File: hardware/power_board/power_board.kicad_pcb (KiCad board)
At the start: 2 copper layers, 104.1 x 77.9 mm, 35 parts, among them J1 MCU, J2 MAINS_IN, J6 HEATER-E, J7 HEATER-N, J8 HEATER-L, K3 HEATER-BOTTOM, K4 HEATER-TOP, Q4 MMBT3904, Q5 MMBT3904, U10 PC817, U6 AMS1117-3.3, U9 PC817

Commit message: v2 Power/Relay PCB
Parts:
- removed D6, D7: LED, LED_THT:LED_D5.0mm_Clear
- removed J6: HEATER-E, TerminalBlock_Dinkle:TerminalBlock_Dinkle_DT-55-B01X-02_P10.00mm
- removed J7: HEATER-N, TerminalBlock_Dinkle:TerminalBlock_Dinkle_DT-55-B01X-02_P10.00mm
- removed R12, R13: 330, Resistor_SMD:R_0805_2012Metric
- added C2: 470uF, Capacitor_THT:CP_Radial_D8.0mm_P3.50mm, F.Cu at (157.1, 92.3)
- added C3: 1uF, Capacitor_THT:CP_Radial_D8.0mm_P3.50mm, F.Cu at (166.4, 92.2)
- added Q1: MMBT3904, Package_TO_SOT_SMD:SOT-23, B.Cu at (126.0, 72.5)
- added R2: 1k, Resistor_SMD:R_0805_2012Metric, B.Cu at (130.1, 71.9)
- D3: renamed from D1; footprint LED_THT:LED_D5.0mm_Clear -> LED_SMD:LED_0805_2012Metric_Pad1.15x1.40mm_HandSolder; moved to B.Cu
- F1: renamed from F3; footprint TE5:FUSE_BK_PCE-5-R -> Fuse:Fuse_Littelfuse_395Series
- J1: footprint Connector_PinHeader_2.54mm:PinHeader_1x04_P2.54mm_Vertical -> Connector_PinHeader_2.54mm:PinHeader_1x06_P2.54mm_Vertical
- J2: footprint TerminalBlock_Dinkle:TerminalBlock_Dinkle_DT-55-B01X-03_P10.00mm -> TerminalBlock_Dinkle:TerminalBlock_Dinkle_DT-55-B01X-02_P10.00mm
- J8: value HEATER-L -> HEATER; footprint TerminalBlock_Dinkle:TerminalBlock_Dinkle_DT-55-B01X-02_P10.00mm -> TerminalBlock_Dinkle:TerminalBlock_Dinkle_DT-55-B01X-03_P10.00mm
- K1: renamed from K4; footprint Relay_THT:Relay_SPDT_RAYEX-L90 -> Relay_THT:Relay_SPST_RAYEX-L90A
- K2: renamed from K3; footprint Relay_THT:Relay_SPDT_RAYEX-L90 -> Relay_THT:Relay_SPST_RAYEX-L90A
- U1: renamed from U9; footprint Package_DIP:DIP-4_W7.62mm -> Package_DIP:DIP-4_W7.62mm_SMDSocket_SmallPads; moved to B.Cu
- U2: renamed from U10; footprint Package_DIP:DIP-4_W7.62mm -> Package_DIP:DIP-4_W7.62mm_SMDSocket_SmallPads; moved to B.Cu
- moved REF** 253.2 mm to (-125.6, 142.2)
- moved REF** 248.7 mm to (-117.5, 141.6)
- moved REF** 175.8 mm to (-136.8, 142.4)
- moved REF** 164.1 mm to (-131.1, 142.2)
- moved J1 156.6 mm to (176.4, 71.2)
- moved C1 151.4 mm to (181.3, 131.2)
- moved C4 138.5 mm to (161.9, 84.0), turned to 0 degrees
- moved D3 136.1 mm to (173.9, 89.4), turned to 0 degrees
- moved U3 133.9 mm to (161.7, 78.1)
- moved C5 130.3 mm to (167.3, 78.2), turned to -90 degrees
- moved R8 127.7 mm to (173.8, 93.5), turned to 0 degrees
- moved L1 127.6 mm to (172.3, 131.5)
- moved RV1 126.3 mm to (155.8, 125.5), turned to 90 degrees
- moved F1 116.1 mm to (155.7, 131.7), turned to 0 degrees
- moved PS1 115.7 mm to (156.0, 103.5), turned to 0 degrees
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- renumbered C4 to C1, C5 to C4, C6 to C5, D9 to D1, D8 to D2, L2 to L1, PS2 to PS1, Q5 to Q2, Q4 to Q3, R8 to R1, R10 to R3, R9 to R5, R11 to R6, R1 to R8, RV2 to RV1, U6 to U3
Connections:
- D1 pad 1: +3.3V -> +5V
- D1 pad 2: Net-(D9-A) -> LED_TOP
- D2 pad 1: +3.3V -> +5V
- D2 pad 2: Net-(D8-A) -> LED_BOTTOM
- J1 pad 1: RELAY_TOP -> LED_BOTTOM
- J1 pad 3: +3.3V -> LED_TOP
- J1 pad 4: GND -> RELAY_TOP
- J2 pad 1: MAINSIN_N -> MAINSIN_L
- J2 pad 2: MAINSIN_L -> MAINSIN_N
- K1 pad A1: +3.3V -> +5V
- K1 pad A2: Net-(D9-A) -> LED_TOP
- K2 pad A1: +3.3V -> +5V
- K2 pad A2: Net-(D8-A) -> LED_BOTTOM
- Q2 pad 3: Net-(D9-A) -> LED_TOP
- Q3 pad 3: Net-(D8-A) -> LED_BOTTOM
- U1 pad 4: +3.3V -> +5V
- U2 pad 4: +3.3V -> +5V
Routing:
- net +3.3V: track 212.2 -> 24.4 mm, vias 2 -> 0
- net LED_BOTTOM: track 0.00 -> 109.7 mm
- net +5V: track 64.5 -> 162.1 mm
- net LED_TOP: track 0.00 -> 68.7 mm
- net Net-(K3-Pad12): track 56.9 -> 0.00 mm
- net RELAY_TOP: track 97.0 -> 51.8 mm, vias 0 -> 2
- net Net-(J8-Pin_1): track 63.2 -> 20.1 mm
- net MAINSIN_N: track 113.4 -> 80.6 mm
- net MAINSIN_E: track 23.9 -> 0.00 mm
- net Net-(D8-A): track 21.2 -> 0.00 mm
- net Net-(D9-A): track 21.0 -> 0.00 mm
- net Net-(R3-Pad1): track 3.61 -> 21.5 mm
- net Net-(R6-Pad1): track 3.79 -> 18.8 mm
- net MAINSIN_L: track 82.3 -> 68.4 mm
- net Net-(D7-K): track 10.2 -> 0.00 mm
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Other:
- board size 104.1 x 77.9 mm -> 101.3 x 70.6 mm
- board text added: "L-BOTTOM"
- board text added: "L-TOP"
- board text added: "N-HEATERS"

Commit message: Refactored PCBs for v2. See README
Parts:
- removed the REF** at (-117.5, 141.6)
- removed the REF** at (-131.1, 142.2)
- removed the REF** at (-136.8, 142.4)
- removed the REF** at (-125.6, 142.2)
- added REF**: MountingHole_2.2mm_M2_DIN965_Pad, MountingHole:MountingHole_2.2mm_M2_DIN965_Pad, F.Cu at (190.8, 136.3)
- added REF**: MountingHole_2.2mm_M2_DIN965_Pad, MountingHole:MountingHole_2.2mm_M2_DIN965_Pad, F.Cu at (97.2, 136.3)
- added REF**: MountingHole_2.2mm_M2_DIN965_Pad, MountingHole:MountingHole_2.2mm_M2_DIN965_Pad, F.Cu at (97.7, 68.9)
- J2: footprint TerminalBlock_Dinkle:TerminalBlock_Dinkle_DT-55-B01X-02_P10.00mm -> TerminalBlock2:HB9500-9.5-2P
- J8: footprint TerminalBlock_Dinkle:TerminalBlock_Dinkle_DT-55-B01X-03_P10.00mm -> TerminalBlock2:HB9500-9.5-3P
- L1: footprint Inductor_THT:Choke_Schaffner_RN204-04-9.0x14.0mm -> Chokes:CHOKE UU9.8
- U1, U2: footprint Package_DIP:DIP-4_W7.62mm_SMDSocket_SmallPads -> PC817XI:SOIC254P975X460-4N
- moved J2 18.8 mm to (128.2, 117.4), turned to 0 degrees
- moved L1 12.3 mm to (177.8, 120.5), turned to -90 degrees
- moved J8 9.50 mm to (96.4, 117.3)
- moved F1 3.04 mm to (157.6, 134.0)
- moved PS1 3.04 mm to (158.0, 105.8)
- moved RV1 3.04 mm to (157.8, 127.8)
- moved C1 2.35 mm to (183.4, 132.3)
- moved C2 1.80 mm to (158.9, 92.3)
- moved D3 1.80 mm to (175.7, 89.4)
- moved R8 1.80 mm to (175.6, 93.5)
- moved K2 1.80 mm to (110.7, 88.2)
- moved C3 1.80 mm to (168.2, 92.2)
- moved K1 1.80 mm to (140.1, 88.3)
- moved R1 0.91 mm to (147.4, 75.3)
- moved C4 0.91 mm to (161.0, 83.9)
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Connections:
- J2 pad 1: MAINSIN_L -> MAINSIN_N
- J2 pad 2: MAINSIN_N -> MAINSIN_L
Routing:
- net Net-(PS1-AC/N): track 28.6 -> 18.9 mm
- net GND: track 168.5 -> 177.4 mm
- net Net-(PS1-AC/L): track 23.2 -> 30.8 mm
- net MAINSIN_L: track 68.4 -> 74.9 mm
- net Net-(J8-Pin_1): track 20.1 -> 15.5 mm
- net MAINSIN_N: track 80.6 -> 84.5 mm
- net +5V: track 162.1 -> 165.6 mm
- net Net-(J8-Pin_2): track 28.7 -> 31.0 mm
- net Net-(C1-Pad1): track 32.9 -> 31.3 mm
- net LED_TOP: track 68.7 -> 69.4 mm
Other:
- board size 101.3 x 70.6 mm -> 98.8 x 72.8 mm

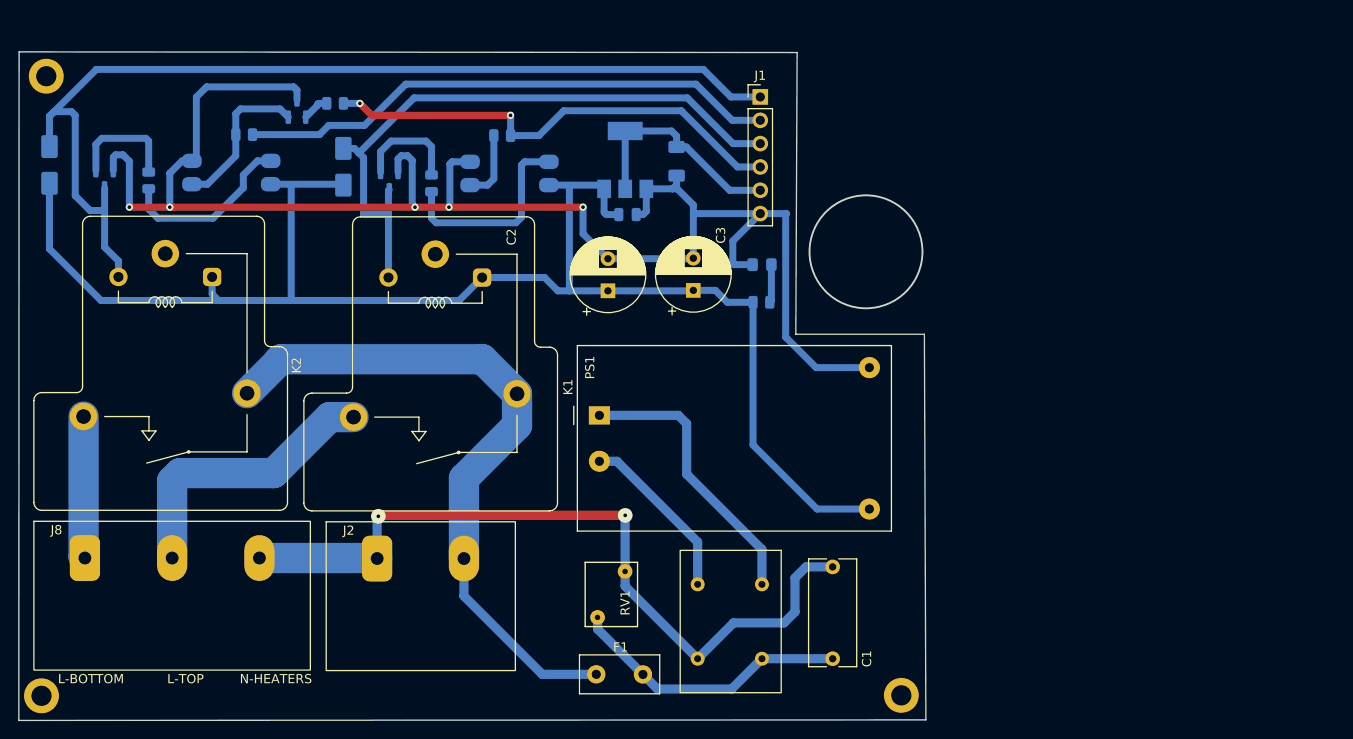
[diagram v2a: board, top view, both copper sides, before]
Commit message: v2 layout changes to fit in bax
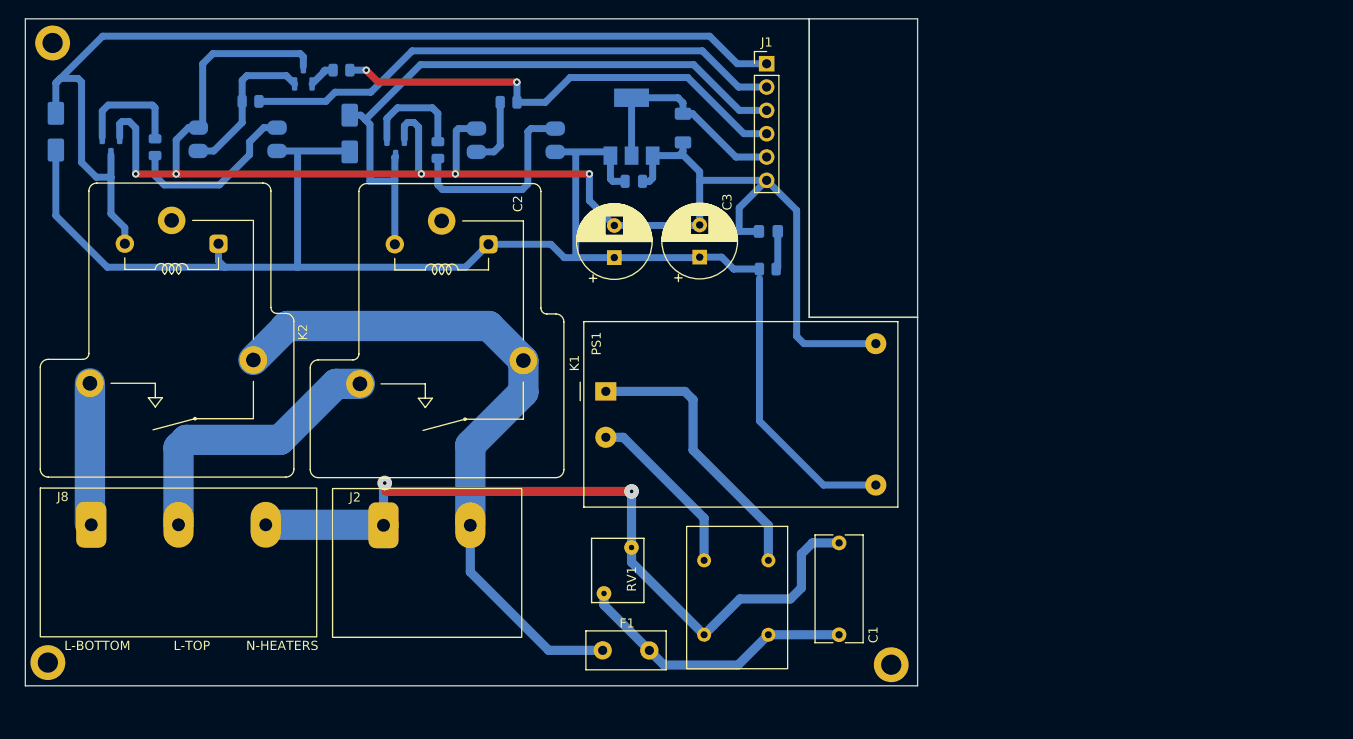
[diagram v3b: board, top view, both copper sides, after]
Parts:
- moved C3 3.69 mm to (168.9, 88.6)
- moved R1 3.69 mm to (148.1, 71.7)
- moved J8 3.69 mm to (97.1, 113.7)
- moved C2 3.69 mm to (159.6, 88.6)
- moved D2 3.69 mm to (98.8, 74.9)
- moved D3 3.69 mm to (176.4, 85.8)
- moved J1 3.69 mm to (176.2, 67.5)
- moved J2 3.69 mm to (128.9, 113.8)
- moved K1 3.69 mm to (140.8, 84.6)
- moved K2 3.69 mm to (111.4, 84.6)
- moved Q1 3.69 mm to (125.7, 68.8)
- moved Q3 3.69 mm to (104.8, 76.5)
- moved R2 3.69 mm to (129.9, 68.2)
- moved R3 3.69 mm to (140.4, 76.9)
- moved R6 3.69 mm to (109.6, 76.6)
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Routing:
- net MAINSIN_L: track 74.9 -> 76.0 mm
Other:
- board size 98.8 x 72.8 mm -> 97.2 x 72.6 mm

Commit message: v2 Boards for fabrication
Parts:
- C1, C2, C3, F1, J1, J2, J8, K1, K2, L1, PS1, REF** (x3), RV1: moved to B.Cu
- C4, C5, D1, D2, D3, Q1, Q2, Q3, R1, R2, R3, R5, R6, R8, U1, U2, U3: moved to F.Cu
- moved J8 93.5 mm to (190.6, 113.7), turned to 180 degrees
- moved REF** 91.8 mm to (97.9, 133.0), turned to 180 degrees
- moved REF** 91.8 mm to (189.7, 132.7), turned to 180 degrees
- moved REF** 90.8 mm to (189.2, 65.3), turned to 180 degrees
- moved D2 90.1 mm to (188.9, 74.9)
- moved C1 80.5 mm to (103.6, 129.7)
- moved Q3 78.1 mm to (182.9, 76.5)
- moved L1 69.3 mm to (109.2, 117.9)
- moved R6 68.5 mm to (178.1, 76.6)
- moved D3 65.1 mm to (111.3, 85.8), turned to 180 degrees
- moved R8 64.9 mm to (111.4, 89.9), turned to 180 degrees
- moved K2 64.9 mm to (176.3, 84.6)
- moved J1 64.7 mm to (111.5, 67.5), turned to 180 degrees
- moved U2 50.5 mm to (169.1, 75.8), turned to 180 degrees
- moved C3 50.1 mm to (118.8, 88.6)
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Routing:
- net MAINSIN_N: track 84.5 -> 83.2 mm
- added copper zone on F.Cu, net (none)
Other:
- outline, holes or cut-outs redrawn

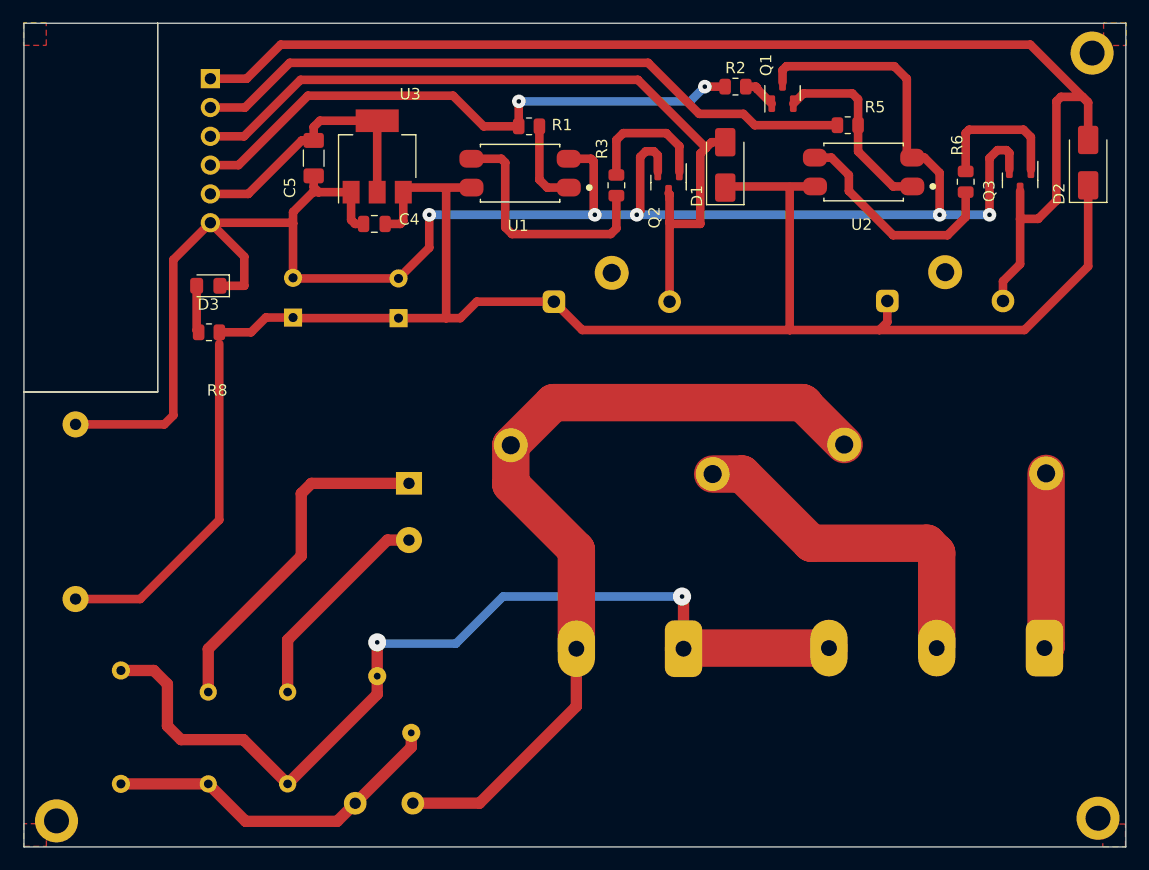
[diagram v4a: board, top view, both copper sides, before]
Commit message: Add missing holes and fabrication marks
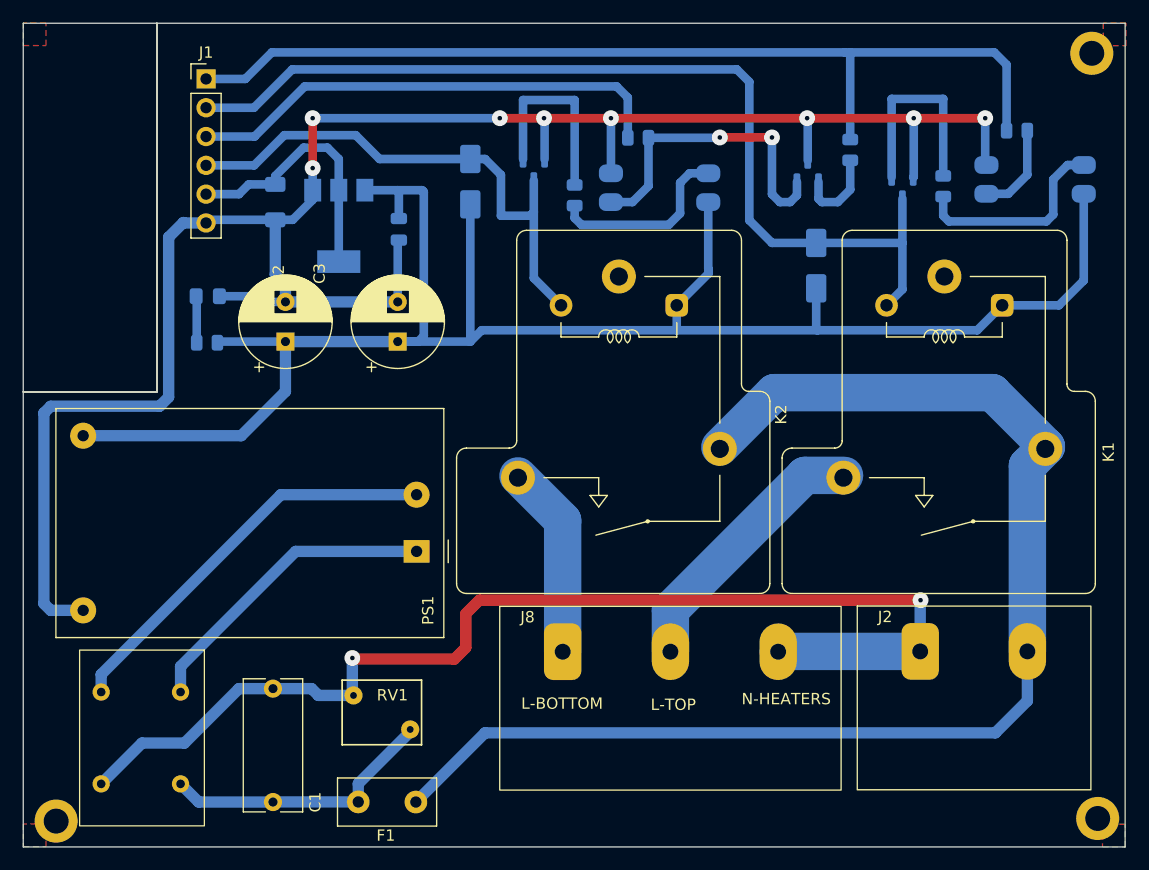
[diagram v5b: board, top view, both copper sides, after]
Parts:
- removed REF** (x3): MountingHole_2.2mm_M2_DIN965_Pad, MountingHole:MountingHole_2.2mm_M2_DIN965_Pad
- added ?: , , F.Cu at (189.7, 132.8)
- added ?: , , F.Cu at (189.2, 65.3)
- added ?: , , F.Cu at (97.9, 133.0)
- C1, C2, C3, F1, J1, J2, J8, L1, PS1, RV1: moved to F.Cu
- C4, C5, D1, D2, D3, Q1, Q2, Q3, R1, R2, R3, R5, R6, R8, U1, U2, U3: moved to B.Cu
- K1: value HEATER-TOP -> BOOST; moved to F.Cu
- K2: value HEATER-BOTTOM -> OFFPEAK; moved to F.Cu
- moved D2 54.5 mm to (134.4, 76.6)
- moved J8 53.6 mm to (137.0, 114.0), turned to 0 degrees
- moved U1 45.4 mm to (184.2, 76.4), turned to 0 degrees
- moved R1 43.0 mm to (182.6, 72.1)
- moved Q3 42.9 mm to (140.0, 75.6)
- moved R6 34.5 mm to (143.6, 77.8)
- moved K1 29.3 mm to (176.2, 85.0)
- moved R3 28.8 mm to (176.1, 77.0)
- moved K2 28.8 mm to (147.5, 85.0)
- moved Q2 20.6 mm to (172.5, 77.2)
- moved R5 18.5 mm to (149.2, 72.7)
- moved U2 18.0 mm to (151.1, 77.1), turned to 0 degrees
- moved C1 13.5 mm to (117.0, 131.3)
- moved D1 12.0 mm to (164.9, 84.0)
- moved R2 11.6 mm to (167.9, 73.8), turned to -90 degrees
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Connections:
- D1 pad 2: LED_TOP -> LED_BOOST
- D2 pad 2: LED_BOTTOM -> LED_OFFPEAK
- J1 pad 1: LED_BOTTOM -> RELAY_BOOST
- J1 pad 2: RELAY_BOTTOM -> LED_BOOST
- J1 pad 3: LED_TOP -> RELAY_OFFPEAK
- J1 pad 4: RELAY_TOP -> LED_OFFPEAK
- K1 pad A2: LED_TOP -> LED_BOOST
- K2 pad A2: LED_BOTTOM -> LED_OFFPEAK
- Q2 pad 3: LED_TOP -> LED_BOOST
- Q3 pad 3: LED_BOTTOM -> LED_OFFPEAK
- R1 pad 2: RELAY_TOP -> RELAY_BOOST
- R2 pad 1: RELAY_TOP -> RELAY_BOOST
- R5 pad 2: RELAY_BOTTOM -> RELAY_OFFPEAK
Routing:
- net LED_BOTTOM: track 110.1 -> 0.00 mm
- net LED_BOOST: track 0.00 -> 86.6 mm
- net RELAY_BOOST: track 0.00 -> 85.5 mm
- net LED_TOP: track 69.4 -> 0.00 mm
- net RELAY_BOTTOM: track 59.2 -> 0.00 mm
- net RELAY_TOP: track 51.8 -> 0.00 mm, vias 2 -> 0
- net LED_OFFPEAK: track 0.00 -> 47.2 mm
- net RELAY_OFFPEAK: track 0.00 -> 43.0 mm
- net MAINSIN_L: track 76.0 -> 113.5 mm
- net MAINSIN_N: track 83.2 -> 100.4 mm
- net Net-(PS1-AC/N): track 18.9 -> 35.9 mm
- net Net-(Q1-E): track 15.9 -> 28.0 mm, vias 0 -> 2
- net Net-(J8-Pin_2): track 31.0 -> 24.0 mm
- net Net-(C1-Pad1): track 31.3 -> 24.6 mm
- net Net-(Q2-B): track 11.6 -> 18.3 mm
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
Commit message: minor layout tweaks
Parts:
- moved D3 0.56 mm to (111.8, 86.5)
- moved R8 0.50 mm to (111.7, 90.8)
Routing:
- net +5V: track 161.5 -> 161.0 mm
